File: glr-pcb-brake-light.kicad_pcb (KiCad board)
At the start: 2 copper layers, 126 x 30 mm, 31 parts, among them J1 Conn_01x04_Pin

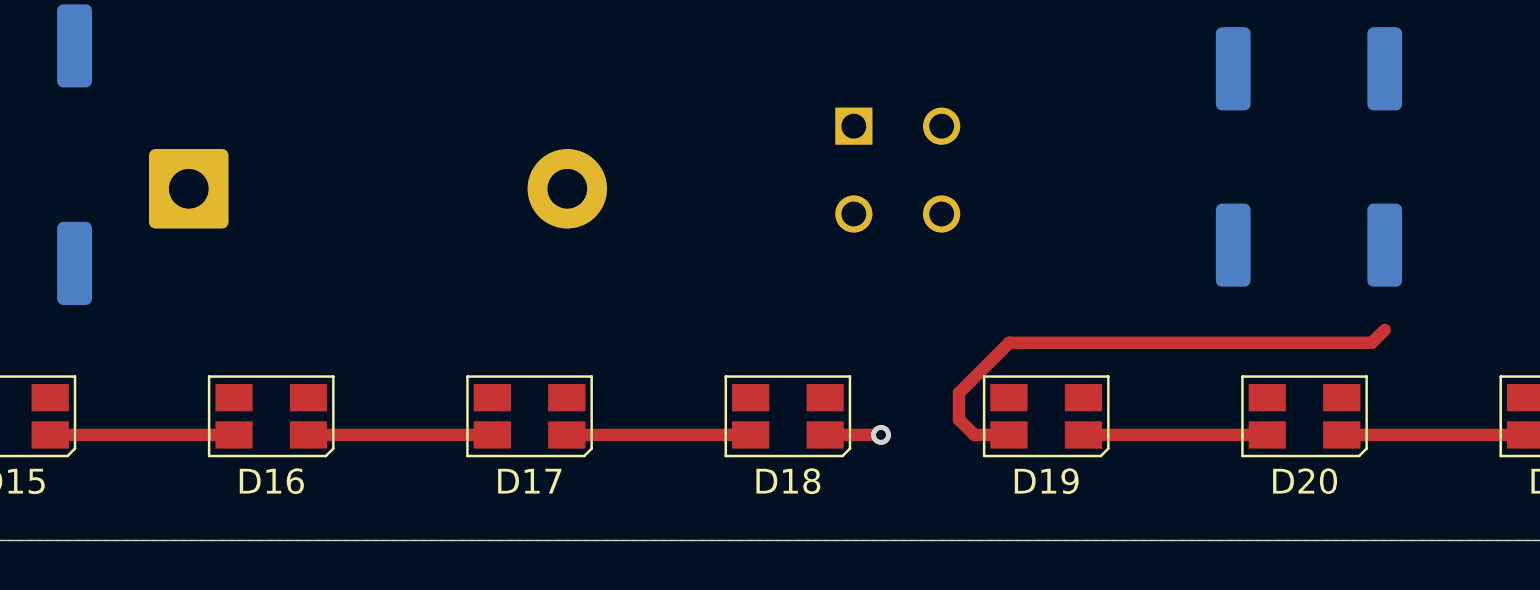
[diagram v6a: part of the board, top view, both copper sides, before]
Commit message: sch überarbeitet für neue leiste
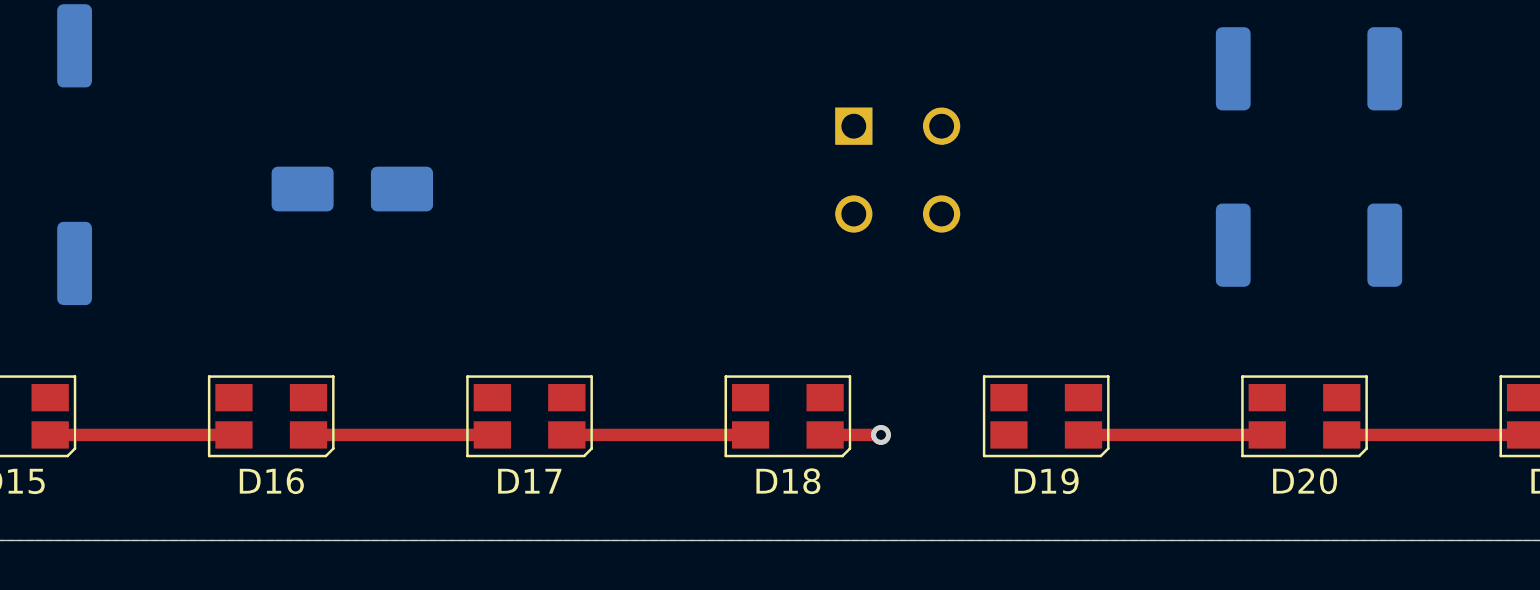
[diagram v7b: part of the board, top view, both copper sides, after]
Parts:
- D25: footprint Diode_THT:D_DO-201AD_P15.24mm_Horizontal -> Diode_SMD:D_SMA
- moved D25 6.58 mm to (141.1, 95.5)
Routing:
- net Net-(D19-A): track 21.5 -> 0.00 mm
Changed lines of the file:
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@@
 		)
 	)
-	(footprint "Diode_THT:D_DO-201AD_P15.24mm_Horizontal"
+	(footprint "Diode_SMD:D_SMA"
 		(layer "B.Cu")
-		(at 134.49 95.48)
-		(descr "Diode, DO-201AD series, Axial, Horizontal, pin pitch=15.24mm, length*diameter=9.5*5.2mm^2, http://www.diodes.com/_files/packages/DO-201AD.pdf")
-		(tags "Diode DO-201AD series Axial Horizontal pin pitch 15.24mm  length 9.5mm diameter 5.2mm")
+		(at 141.074 95.49)
+		(descr "Diode SMA (DO-214AC)")
+		(tags "Diode SMA (DO-214AC)")
 		(property "Reference" "D25"
-			(at 2.62 -4 0)
+			(at 0 2.5 180)
 			(layer "B.SilkS")
 			(effects
@@
 		)
 		(property "Value" "1N5822"
-			(at 7.62 -3.72 0)
+			(at 0 -2.6 180)
 			(layer "B.Fab")
 			(effects
@@
 			)
 		)
-		(property "Datasheet" "http://www.vishay.com/docs/88526/1n5820.pdf"
-			(at 0 0 0)
+		(property "Datasheet" "kicad-embed://DS_stps1l60.pdf"
+			(at 0 0 180)
+			(unlocked yes)
 			(layer "B.Fab")
 			(hide yes)
@@
 				(font
 					(size 1.27 1.27)
-				)
-				(justify mirror)
-			)
-		)
-		(property "Description" "40V 3A Schottky Barrier Rectifier Diode, DO-201AD"
-			(at 0 0 0)
+					(thickness 0.15)
+				)
+				(justify mirror)
+			)
+		)
+		(property "Description" "60V 1A Verpolschutz Diode"
+			(at 0 0 180)
+			(unlocked yes)
 			(layer "B.Fab")
 			(hide yes)
@@
 				(font
 					(size 1.27 1.27)
-				)
-				(justify mirror)
-			)
-		)
-		(property "KiLib_Generator" "diode/THT"
-			(at 0 0 0)
-			(layer "B.SilkS")
-			(hide yes)
-			(effects
-				(font
-					(size 1 1)
 					(thickness 0.15)
 				)
@@
 			)
 		)
-		(attr through_hole)
+		(attr smd)
 		(duplicate_pad_numbers_are_jumpers no)
 		(fp_line
-			(start 1.84 0)
-			(end 2.75 0)
-			(stroke
-				(width 0.12)
-				(type solid)
-			)
-			(layer "B.SilkS")
-		)
-		(fp_line
-			(start 4.175 2.72)
-			(end 4.175 -2.72)
-			(stroke
-				(width 0.12)
-				(type solid)
-			)
-			(layer "B.SilkS")
-		)
-		(fp_line
-			(start 4.295 2.72)
-			(end 4.295 -2.72)
-			(stroke
-				(width 0.12)
-				(type solid)
-			)
-			(layer "B.SilkS")
-		)
-		(fp_line
-			(start 4.415 2.72)
-			(end 4.415 -2.72)
-			(stroke
-				(width 0.12)
-				(type solid)
-			)
-			(layer "B.SilkS")
-		)
-		(fp_line
-			(start 13.4 0)
-			(end 12.49 0)
-			(stroke
-				(width 0.12)
-				(type solid)
-			)
-			(layer "B.SilkS")
-		)
-		(fp_rect
-			(start 2.75 2.72)
-			(end 12.49 -2.72)
-			(stroke
-				(width 0.12)
-				(type solid)
-			)
-			(fill no)
-			(layer "B.SilkS")
-		)
-		(fp_rect
-			(start -1.85 2.85)
-			(end 17.09 -2.85)
+			(start -3.51 -1.65)
+			(end 2 -1.65)
+			(stroke
+				(width 0.12)
+				(type solid)
+			)
+			(layer "B.SilkS")
+		)
+		(fp_line
+			(start -3.51 1.65)
+			(end -3.51 -1.65)
+			(stroke
+				(width 0.12)
+				(type solid)
+			)
+			(layer "B.SilkS")
+		)
+		(fp_line
+			(start -3.51 1.65)
+			(end 2 1.65)
+			(stroke
+				(width 0.12)
+				(type solid)
+			)
+			(layer "B.SilkS")
+		)
+		(fp_line
+			(start -3.5 -1.75)
+			(end -3.5 1.75)
 			(stroke
 				(width 0.05)
 				(type solid)
 			)
-			(fill no)
 			(layer "B.CrtYd")
 		)
 		(fp_line
-			(start 0 0)
-			(end 2.87 0)
-			(stroke
-				(width 0.1)
-				(type solid)
-			)
-			(layer "B.Fab")
-		)
-		(fp_line
-			(start 4.195 2.6)
-			(end 4.195 -2.6)
-			(stroke
-				(width 0.1)
-				(type solid)
-			)
-			(layer "B.Fab")
-		)
-		(fp_line
-			(start 4.295 2.6)
-			(end 4.295 -2.6)
-			(stroke
-				(width 0.1)
-				(type solid)
-			)
-			(layer "B.Fab")
-		)
-		(fp_line
-			(start 4.395 2.6)
-			(end 4.395 -2.6)
-			(stroke
-				(width 0.1)
-				(type solid)
-			)
-			(layer "B.Fab")
-		)
-		(fp_line
-			(start 15.24 0)
-			(end 12.37 0)
-			(stroke
-				(width 0.1)
-				(type solid)
-			)
-			(layer "B.Fab")
-		)
-		(fp_rect
-			(start 2.87 2.6)
-			(end 12.37 -2.6)
-			(stroke
-				(width 0.1)
-				(type solid)
-			)
-			(fill no)
-			(layer "B.Fab")
-		)
-		(fp_text user "K"
-			(at 0 2.6 0)
-			(layer "B.SilkS")
+			(start -3.5 1.75)
+			(end 3.5 1.75)
+			(stroke
+				(width 0.05)
+				(type solid)
+			)
+			(layer "B.CrtYd")
+		)
+		(fp_line
+			(start 3.5 -1.75)
+			(end -3.5 -1.75)
+			(stroke
+				(width 0.05)
+				(type solid)
+			)
+			(layer "B.CrtYd")
+		)
+		(fp_line
+			(start 3.5 1.75)
+			(end 3.5 -1.75)
+			(stroke
+				(width 0.05)
+				(type solid)
+			)
+			(layer "B.CrtYd")
+		)
+		(fp_line
+			(start -2.3 -1.5)
+			(end -2.3 1.5)
+			(stroke
+				(width 0.1)
+				(type solid)
+			)
+			(layer "B.Fab")
+		)
+		(fp_line
+			(start -0.64944 -0.00102)
+			(end -1.55114 -0.00102)
+			(stroke
+				(width 0.1)
+				(type solid)
+			)
+			(layer "B.Fab")
+		)
+		(fp_line
+			(start -0.64944 -0.00102)
+			(end 0.50118 -0.75032)
+			(stroke
+				(width 0.1)
+				(type solid)
+			)
+			(layer "B.Fab")
+		)
+		(fp_line
+			(start -0.64944 -0.00102)
+			(end 0.50118 0.79908)
+			(stroke
+				(width 0.1)
+				(type solid)
+			)
+			(layer "B.Fab")
+		)
+		(fp_line
+			(start -0.64944 0.79908)
+			(end -0.64944 -0.80112)
+			(stroke
+				(width 0.1)
+				(type solid)
+			)
+			(layer "B.Fab")
+		)
+		(fp_line
+			(start 0.50118 -0.75032)
+			(end 0.50118 0.79908)
+			(stroke
+				(width 0.1)
+				(type solid)
+			)
+			(layer "B.Fab")
+		)
+		(fp_line
+			(start 0.50118 -0.00102)
+			(end 1.4994 -0.00102)
+			(stroke
+				(width 0.1)
+				(type solid)
+			)
+			(layer "B.Fab")
+		)
+		(fp_line
+			(start 2.3 -1.5)
+			(end -2.3 -1.5)
+			(stroke
+				(width 0.1)
+				(type solid)
+			)
+			(layer "B.Fab")
+		)
+		(fp_line
+			(start 2.3 1.5)
+			(end -2.3 1.5)
+			(stroke
+				(width 0.1)
+				(type solid)
+			)
+			(layer "B.Fab")
+		)
+		(fp_line
+			(start 2.3 1.5)
+			(end 2.3 -1.5)
+			(stroke
+				(width 0.1)
+				(type solid)
+			)
+			(layer "B.Fab")
+		)
+		(fp_text user "${REFERENCE}"
+			(at 0 2.5 180)
+			(layer "B.Fab")
 			(effects
 				(font
@@
 			)
 		)
-		(fp_text user "K"
-			(at 0 2.6 0)
-			(layer "B.Fab")
-			(effects
-				(font
-					(size 1 1)
-					(thickness 0.15)
-				)
-				(justify mirror)
-			)
-		)
-		(fp_text user "${REFERENCE}"
-			(at 8.3325 0 0)
-			(layer "B.Fab")
-			(effects
-				(font
-					(size 1 1)
-					(thickness 0.15)
-				)
-				(justify mirror)
-			)
-		)
-		(pad "1" thru_hole roundrect
-			(at 0 0)
-			(size 3.2 3.2)
-			(drill 1.6)
-			(layers "*.Cu" "*.Mask")
-			(remove_unused_layers no)
-			(roundrect_rratio 0.078125)
+		(pad "1" smd roundrect
+			(at -2 0)
+			(size 2.5 1.8)
+			(layers "B.Cu" "B.Mask" "B.Paste")
+			(roundrect_rratio 0.1388888889)
 			(net "Net-(D25-K)")
 			(pinfunction "K_1")
 			(pintype "passive")
 		)
-		(pad "2" thru_hole circle
-			(at 15.24 0)
-			(size 3.2 3.2)
-			(drill 1.6)
-			(layers "*.Cu" "*.Mask")
-			(remove_unused_layers no)
+		(pad "2" smd roundrect
+			(at 2 0)
+			(size 2.5 1.8)
+			(layers "B.Cu" "B.Mask" "B.Paste")
+			(roundrect_rratio 0.1388888889)
 			(net "+24V")
 			(pinfunction "A_2")
@@
 		)
 		(embedded_fonts no)
-		(model "${KICAD10_3DMODEL_DIR}/Diode_THT.3dshapes/D_DO-201AD_P15.24mm_Horizontal.step"
+		(model "${KICAD10_3DMODEL_DIR}/Diode_SMD.3dshapes/D_SMA.step"
 			(offset
 				(xyz 0 0 0)
@@
 	)
 	(segment
-		(start 166.12 105.39)
-		(end 165.5 104.77)
-		(width 0.5)
-		(layer "F.Cu")
-		(net "Net-(D19-A)")
-	)
-	(segment
-		(start 182.12 101.68)
-		(end 182.64 101.16)
-		(width 0.5)
-		(layer "F.Cu")
-		(net "Net-(D19-A)")
-	)
-	(segment
-		(start 165.5 103.7)
-		(end 167.52 101.68)
-		(width 0.5)
-		(layer "F.Cu")
-		(net "Net-(D19-A)")
-	)
-	(segment
-		(start 165.5 104.77)
-		(end 165.5 103.7)
-		(width 0.5)
-		(layer "F.Cu")
-		(net "Net-(D19-A)")
-	)
-	(segment
-		(start 167.51 105.39)
-		(end 166.12 105.39)
-		(width 0.5)
-		(layer "F.Cu")
-		(net "Net-(D19-A)")
-	)
-	(segment
-		(start 167.52 101.68)
-		(end 182.12 101.68)
-		(width 0.5)
-		(layer "F.Cu")
-		(net "Net-(D19-A)")
-	)
-	(segment

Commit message: leds hinzugefügt
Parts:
- added D26: LED, GLR_KiCad_Library:LED_Avago_PLCC4_3.2x2.8mm_CW, F.Cu at (25.4, 164.4)
- added D27: LED, GLR_KiCad_Library:LED_Avago_PLCC4_3.2x2.8mm_CW, F.Cu at (25.4, 168.8)
- added D28: LED, GLR_KiCad_Library:LED_Avago_PLCC4_3.2x2.8mm_CW, F.Cu at (25.4, 173.1)
- added D29: LED, GLR_KiCad_Library:LED_Avago_PLCC4_3.2x2.8mm_CW, F.Cu at (25.4, 177.5)
- added D30: LED, GLR_KiCad_Library:LED_Avago_PLCC4_3.2x2.8mm_CW, F.Cu at (25.4, 181.8)
- added D31: LED, GLR_KiCad_Library:LED_Avago_PLCC4_3.2x2.8mm_CW, F.Cu at (25.4, 186.2)
- added R5: 220, Resistor_SMD:R_2512_6332Metric_Pad1.40x3.35mm_HandSolder, F.Cu at (33.0, 164.7)
- D0: renamed from D25; value 1N5822 -> STPS1L60
